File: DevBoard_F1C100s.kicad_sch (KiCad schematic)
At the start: 25 parts, among them J101 USB_C_Receptacle_USB2.0_16P, U101 F1C100s, U102 AMS1117, U103 AMS1117-3.3, U104 TPS562201DDCT

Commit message: Schematic: Finished
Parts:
- removed TP101: TestPoint_Small, TestPoint:TestPoint_Pad_D1.0mm, symbol Connector:TestPoint_Small
- added C108, C110, C113: 10uf, Capacitor_SMD:C_0603_1608Metric_Pad1.08x0.95mm_HandSolder, symbol Device:C_Small
- added C109, C112, C115, C116: 0.1uf, Capacitor_SMD:C_0603_1608Metric_Pad1.08x0.95mm_HandSolder, symbol Device:C_Small
- added C111, C114: 10pf, Capacitor_SMD:C_0603_1608Metric_Pad1.08x0.95mm_HandSolder, symbol Device:C_Small
- added J102: Conn_01x22, Connector_PinHeader_1.00mm:PinHeader_1x22_P1.00mm_Vertical_SMD_Pin1Left, symbol Connector_Generic:Conn_01x22
- added J103: Conn_01x11, Connector_PinHeader_1.00mm:PinHeader_1x11_P1.00mm_Vertical_SMD_Pin1Left, symbol Connector_Generic:Conn_01x11
- added J104: SD_Card, Connector_PinHeader_1.00mm:PinHeader_1x06_P1.00mm_Vertical_SMD_Pin1Left, symbol Connector_Generic:Conn_01x06
- added J105: UART0, Connector_PinHeader_1.00mm:PinHeader_1x04_P1.00mm_Vertical_SMD_Pin1Left, symbol Connector_Generic:Conn_01x04
- added J106: Conn_01x10, Connector_PinHeader_1.00mm:PinHeader_1x10_P1.00mm_Vertical_SMD_Pin1Left, symbol Connector_Generic:Conn_01x10
- added J107: Conn_01x04, Connector_PinHeader_1.00mm:PinHeader_1x04_P1.00mm_Vertical_SMD_Pin1Left, symbol Connector_Generic:Conn_01x04
- added J108: Conn_01x05, Connector_PinHeader_1.00mm:PinHeader_1x05_P1.00mm_Vertical_SMD_Pin1Left, symbol Connector_Generic:Conn_01x05
- added J109: Conn_01x02, Connector_PinHeader_1.00mm:PinHeader_1x02_P1.00mm_Vertical_SMD_Pin1Left, symbol Connector_Generic:Conn_01x02
- added R107: 10k, Resistor_SMD:R_0201_0603Metric_Pad0.64x0.40mm_HandSolder, symbol Device:R_Small
- added R108, R109, R110, R111, R112, R113: 5.1K, Resistor_SMD:R_0201_0603Metric_Pad0.64x0.40mm_HandSolder, symbol Device:R_Small
- added SW101, SW102: SW1, Button_Switch_SMD:SW_SPST_CK_RS282G05A3, symbol Switch:SW_Push
- added SW103: SW2, Button_Switch_SMD:SW_SPST_CK_RS282G05A3, symbol Switch:SW_Push
- added SW104: SW3, Button_Switch_SMD:SW_SPST_CK_RS282G05A3, symbol Switch:SW_Push
- added SW105: RESET, Button_Switch_SMD:SW_SPST_CK_RS282G05A3, symbol Switch:SW_Push
- added U104: W25Q16JVSS, Package_SO:SOIC-8_5.3x5.3mm_P1.27mm, symbol Memory_Flash:W25Q16JVSS
- added Y101: 24Mhz, Crystal:Crystal_SMD_3225-4Pin_3.2x2.5mm_HandSoldering, symbol Device:Crystal_GND24
- F101: footprint (none) -> Jumper:SolderJumper-2_P1.3mm_Open_TrianglePad1.0x1.5mm
- U103: renamed from U104; footprint DDC0006A_N -> TPS562201DDCT:DDC0006A_N
- U105: renamed from U101; footprint (none) -> F1C100s:QFN-88_EP_10x10_Pitch0.4mm
- renumbered C105 to C102, C107 to C103, C103 to C105, C102 to C106, C106 to C107, JP102 to JP101, R104 to R102, R102 to R103, R103 to R104, TP103 to TP101, TP104 to TP103, U102 to U101, U103 to U102
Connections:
- net 1V1: now also U105.22 (VCC_CORE), U105.35 (VCC_CORE), U105.71 (VCC_CORE), C113.1, C115.1
- net 2V6: now also U105.30 (VCC_DRAM), U105.31 (VCC_DRAM), U105.32 (VCC_DRAM), U105.34 (VCC_DRAM), U105.36 (VCC_DRAM), U105.80 (AVCC), C110.1, C112.1, R112.1
- net 3V3: now also U105.20 (VCC_IO), U105.4 (HPVCC), U105.5 (VCC_IO), U105.50 (VCC_IO), U105.73 (TV_VCC), C108.1, C109.1, J105.1 (Pin_1), R107.1, SW101.2, SW102.2, SW103.2, SW104.2, U104.3 (~{WP}/IO_{2}), U104.7 (~{HOLD}/~{RESET}/IO_{3}), U104.8 (VCC)
- net GND: now also U105.74 (TVGND), U105.82 (AGND), C108.2, C109.2, C110.2, C111.2, C112.2, C113.2, C114.1, C115.2, C116.2, J105.4 (Pin_4), R108.2, R109.2, R110.2, R111.2, R113.2, SW105.1, U104.4 (GND), Y101.2, Y101.4
- net PWR_F: now also U105.67 (USB_VCC)
- net USB_N: now also U105.68 (USB_DM)
- net USB_P: now also U105.69 (USB_DP)
- net HPL: now reaches U105.1 (HPL)
- net HPL: now also J106.8 (Pin_8)
- net PD4: now reaches U105.10 (PD4)
- net PD4: now also J102.5 (Pin_5)
- net PD5: now reaches U105.11 (PD5)
- net PD5: now also J102.6 (Pin_6)
- net PD6: now reaches U105.12 (PD6)
- net PD6: now also J102.7 (Pin_7)
- net PD7: now reaches U105.13 (PD7)
- net PD7: now also J102.8 (Pin_8)
- net PD8: now reaches U105.14 (PD8)
- net PD8: now also J102.9 (Pin_9)
- net PD9: now reaches U105.15 (PD9)
- net PD9: now also J102.10 (Pin_10)
- net PD10: now reaches U105.16 (PD10)
- net PD10: now also J102.11 (Pin_11)
- net PD11: now reaches U105.17 (PD11)
- net PD11: now also J102.12 (Pin_12)
- net PD12: now reaches U105.18 (PD12)
- net PD12: now also J102.13 (Pin_13)
- net PD13: now reaches U105.19 (PD13)
- net PD13: now also J102.14 (Pin_14)
- net HPCOMFB: now reaches U105.2 (HPCOMFB)
- net HPCOMFB: now also J106.10 (Pin_10)
- net PD14: now reaches U105.21 (PD14)
- net PD14: now also J102.15 (Pin_15)
- net PD15: now reaches U105.23 (PD15)
- net PD15: now also J102.16 (Pin_16)
- net PD16: now reaches U105.24 (PD16)
- net PD16: now also J102.17 (Pin_17)
- net PD17: now reaches U105.25 (PD17)
- net PD17: now also J102.18 (Pin_18)
- net PD18: now reaches U105.26 (PD18)
- net PD18: now also J102.19 (Pin_19)
- net PD19: now reaches U105.27 (PD19)
- net PD19: now also J102.20 (Pin_20)
- net PD20: now reaches U105.28 (PD20)
- net PD20: now also J102.21 (Pin_21)
- net PD21: now reaches U105.29 (PD21)
- net PD21: now also J102.22 (Pin_22)
- net HPCOM: now reaches U105.3 (HPCOM)
- net HPCOM: now also J106.9 (Pin_9)
- net SVREF: now reaches U105.33 (SVREF)
- net SVREF: now also J109.2 (Pin_2), R112.2, R113.1
- net SW3: now reaches U105.37 (PE12)
- net SW3: now also J103.11 (Pin_11), R111.1, SW104.1
- net SW2: now reaches U105.38 (PE11)
- net SW2: now also J103.10 (Pin_10), R110.1, SW103.1
- net SW1: now reaches U105.39 (PE10)
- net SW1: now also J103.9 (Pin_9), R109.1, SW102.1
- net SW0: now reaches U105.40 (PE9)
- net SW0: now also J103.8 (Pin_8), R108.1, SW101.1
- net PE8: now reaches U105.41 (PE8)
- net PE8: now also J103.7 (Pin_7)
- net PE7: now reaches U105.42 (PE7)
- net PE7: now also J103.6 (Pin_6)
- net PE6: now reaches U105.43 (PE6)
- net PE6: now also J103.5 (Pin_5)
- net PE5: now reaches U105.44 (PE5)
- net PE5: now also J103.4 (Pin_4)
- net PE4: now reaches U105.45 (PE4)
- net PE4: now also J103.3 (Pin_3)
- net PE3: now reaches U105.46 (PE3)
- net PE3: now also J103.2 (Pin_2)
- net PE2: now reaches U105.47 (PE2)
- net PE2: now also J103.1 (Pin_1)
- net UART0_TX: now reaches U105.48 (PE1)
- net UART0_TX: now also J105.3 (Pin_3)
- net UART0_RX: now reaches U105.49 (PE0)
- net UART0_RX: now also J105.2 (Pin_2)
- net HOSCI: now reaches U105.51 (HOSCI)
- net HOSCI: now also C111.1, Y101.1
- net HOSCO: now reaches U105.52 (HOSCO)
- net HOSCO: now also C114.2, Y101.3
- net SDC0_D2: now reaches U105.53 (PF5)
- net SDC0_D2: now also J104.6 (Pin_6)
- net SDC0_D3: now reaches U105.54 (PF4)
- net SDC0_D3: now also J104.5 (Pin_5)
- net SDC0_CMD: now reaches U105.55 (PF3)
- net SDC0_CMD: now also J104.4 (Pin_4)
- net SDC0_CLK: now reaches U105.56 (PF2)
- net SDC0_CLK: now also J104.3 (Pin_3)
- net SDC0_D0: now reaches U105.57 (PF1)
- net SDC0_D0: now also J104.2 (Pin_2)
- net SDC0_D1: now reaches U105.58 (PF0)
- net SDC0_D1: now also J104.1 (Pin_1)
- net SPI0_CLK: now reaches U105.59 (PC0)
- net SPI0_CLK: now also U104.6 (CLK)
- net PD0: now reaches U105.6 (PD0)
- net PD0: now also J102.1 (Pin_1)
- net SPI0_CS: now reaches U105.60 (PC1)
- net SPI0_CS: now also U104.1 (~{CS})
- net SPI0_MISO: now reaches U105.61 (PC2)
- net SPI0_MISO: now also U104.2 (DO/IO_{1})
- net SPI0_MOSI: now reaches U105.62 (PC3)
- net SPI0_MOSI: now also U104.5 (DI/IO_{0})
- net TPY2: now reaches U105.63 (TPY2)
- net TPY2: now also J107.1 (Pin_1)
- net TPY1: now reaches U105.64 (TPY1)
- net TPY1: now also J107.2 (Pin_2)
- net TPX2: now reaches U105.65 (TPX2)
- net TPX2: now also J107.3 (Pin_3)
- net TPX1: now reaches U105.66 (TPX1)
- net TPX1: now also J107.4 (Pin_4)
- net PD1: now reaches U105.7 (PD1)
- net PD1: now also J102.2 (Pin_2)
- net RESET: now reaches U105.70 (RESET)
- net RESET: now also C116.1, R107.2, SW105.2
- net TVOUT: now reaches U105.72 (TVOUT)
- net TVOUT: now also J108.1 (Pin_1)
- net TV_VRN: now reaches U105.75 (TV_VRN)
- net TV_VRN: now also J108.2 (Pin_2)
- net TV_VRP: now reaches U105.76 (TV_VRP)
- net TV_VRP: now also J108.3 (Pin_3)
- net TVIN1: now reaches U105.77 (TVIN1)
- net TVIN1: now also J108.4 (Pin_4)
- net TVIN0: now reaches U105.78 (TVIN0)
- net TVIN0: now also J108.5 (Pin_5)
- net LRADC0: now reaches U105.79 (LRADC0)
- net LRADC0: now also J109.1 (Pin_1)
- net PD2: now reaches U105.8 (PD2)
- net PD2: now also J102.3 (Pin_3)
- net VRA1: now reaches U105.81 (VRA1)
- net VRA1: now also J106.1 (Pin_1)
- net VRA2: now reaches U105.83 (VRA2)
- net VRA2: now also J106.2 (Pin_2)
- net FMINL: now reaches U105.84 (FMINL)
- net FMINL: now also J106.3 (Pin_3)
- net FMINR: now reaches U105.85 (FMINR)
- net FMINR: now also J106.4 (Pin_4)
- net LINL: now reaches U105.86 (LINL)
- net LINL: now also J106.5 (Pin_5)
- net MICIN: now reaches U105.87 (MICIN)
- net MICIN: now also J106.6 (Pin_6)
- net HPR: now reaches U105.88 (HPR)
- net HPR: now also J106.7 (Pin_7)
- net PD3: now reaches U105.9 (PD3)
- net PD3: now also J102.4 (Pin_4)
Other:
- note added: "Power VCORE: 1.1V 2A VIO: 3.3V 1A VDRAM: 2.6V 1A"
- moved on the sheet: U105

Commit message: Routing: WIP
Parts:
- removed J107: Conn_01x04, Connector_PinHeader_1.00mm:PinHeader_1x04_P1.00mm_Vertical_SMD_Pin1Left, symbol Connector_Generic:Conn_01x04
- removed TP101, TP102, TP103: TestPoint_Small, TestPoint:TestPoint_Pad_D1.0mm, symbol Connector:TestPoint_Small
- R101, R102, R103, R104, R105, R106, R107, R108, R109, R110, R111, R112, R113: footprint Resistor_SMD:R_0201_0603Metric_Pad0.64x0.40mm_HandSolder -> Resistor_SMD:R_0603_1608Metric_Pad0.98x0.95mm_HandSolder
- SW101: value SW1 -> SW0
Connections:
- net TPX1: no longer names the net of U105.66 (TPX1)
- net TPX2: no longer names the net of U105.65 (TPX2)
- net TPY1: no longer names the net of U105.64 (TPY1)
- net TPY2: no longer names the net of U105.63 (TPY2)
- no-connect marks 2 -> 6

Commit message: Layout: Almost complete
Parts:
- removed F101: 5V 2A, Jumper:SolderJumper-2_P1.3mm_Open_TrianglePad1.0x1.5mm, symbol Device:Polyfuse_Small
- removed J109: Conn_01x02, Connector_PinHeader_1.00mm:PinHeader_1x02_P1.00mm_Vertical_SMD_Pin1Left, symbol Connector_Generic:Conn_01x02
- added TP1, TP2: TestPoint, TestPoint:TestPoint_Pad_D1.0mm, symbol Connector:TestPoint
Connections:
- net VBUS is gone; now on net VUSB: J101.A4 (VBUS), J101.A9 (VBUS), J101.B4 (VBUS), J101.B9 (VBUS)
- net LRADC0: now also TP1.1
- net SVREF: now also TP2.1
- net PWR_F renamed VUSB

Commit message: Finish design
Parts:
- removed J104: SD_Card, Connector_PinHeader_1.00mm:PinHeader_1x06_P1.00mm_Vertical_SMD_Pin1Left, symbol Connector_Generic:Conn_01x06
- added J104: Micro_SD_Card_Det1, sd_card:sd_card_10p, symbol sd_card:Micro_SD_Card_Det1
- added R114, R115, R116, R117, R118, R119: 10k, Resistor_SMD:R_0603_1608Metric_Pad0.98x0.95mm_HandSolder, symbol Device:R_Small
- added TP3: TestPoint, TestPoint:TestPoint_Pad_D1.0mm, symbol Connector:TestPoint
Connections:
- net 3V3: now also J104.4 (VDD), R114.1, R115.1, R116.1, R117.1, R118.1, R119.1
- net GND: now also J104.10 (SHIELD), J104.6 (VSS)
- net SDC0_CLK: now also J104.5 (CLK), R117.2
- net SDC0_CMD: now also J104.3 (CMD), R116.2
- net SDC0_D0: now also J104.7 (DAT0), R118.2
- net SDC0_D1: now also J104.8 (DAT1), R119.2
- net SDC0_D2: now also J104.1 (DAT2), R114.2
- net SDC0_D3: now also J104.2 (DAT3/CD), R115.2
- new net: J104.9 (DET), TP3.1
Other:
- moved on the sheet: C111, C114, J105, R112, R113, TP1, TP2, Y101

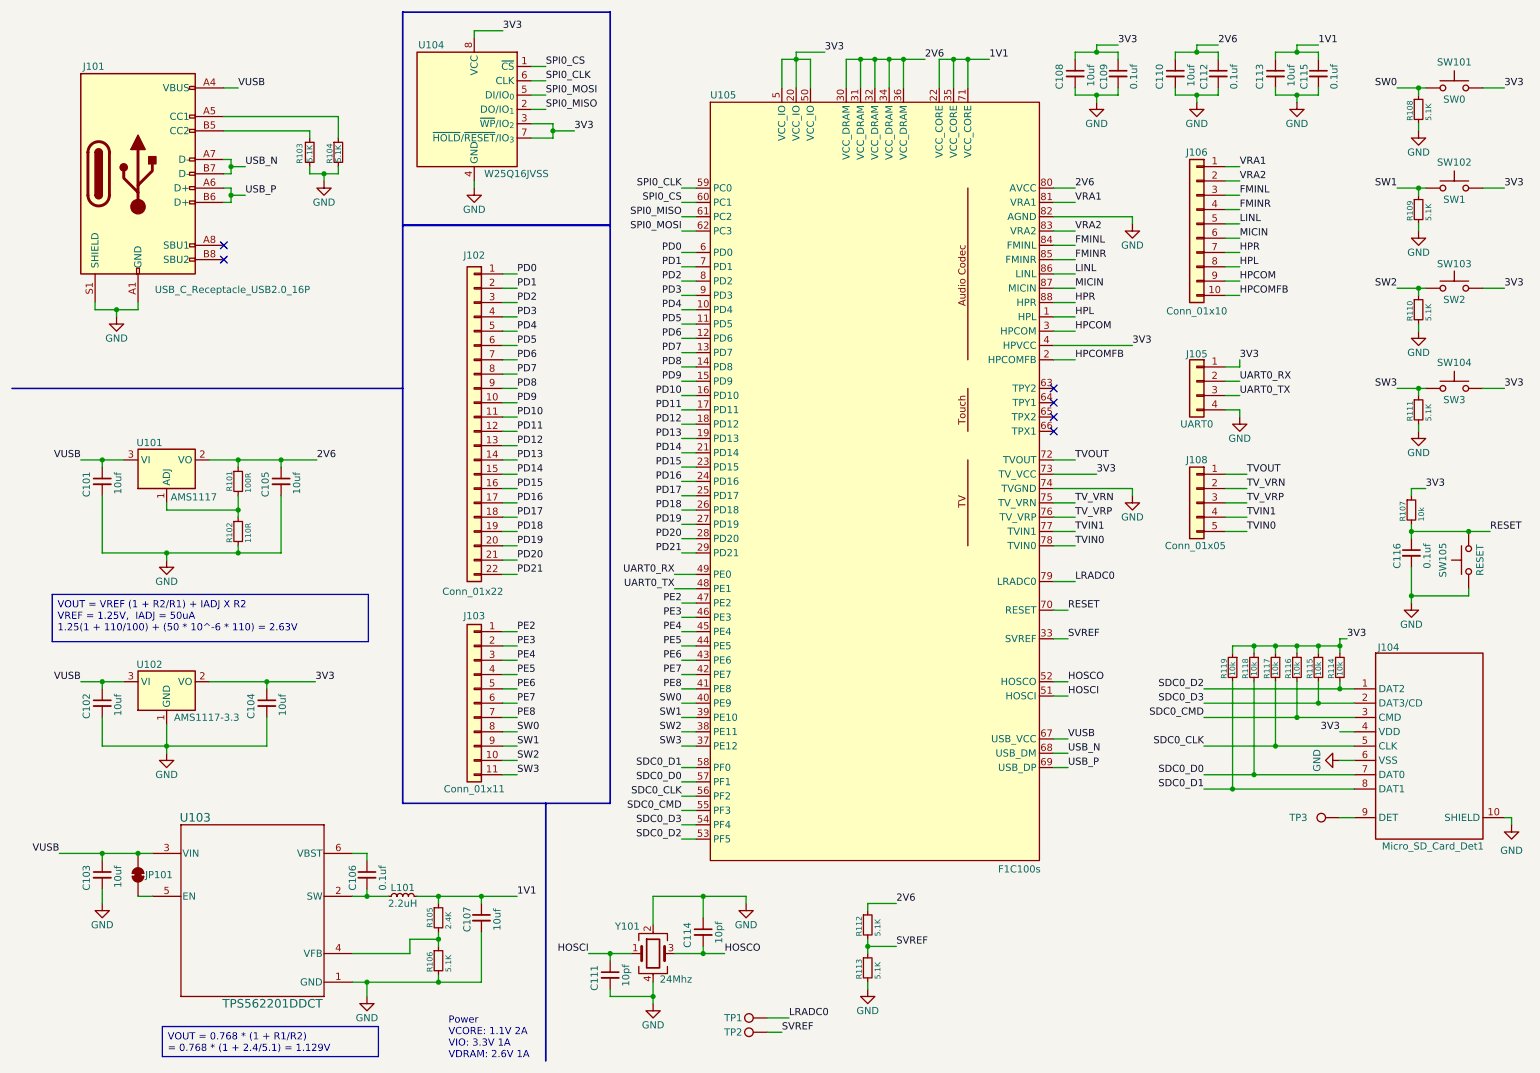
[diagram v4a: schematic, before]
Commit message: Fix ground pour clearance
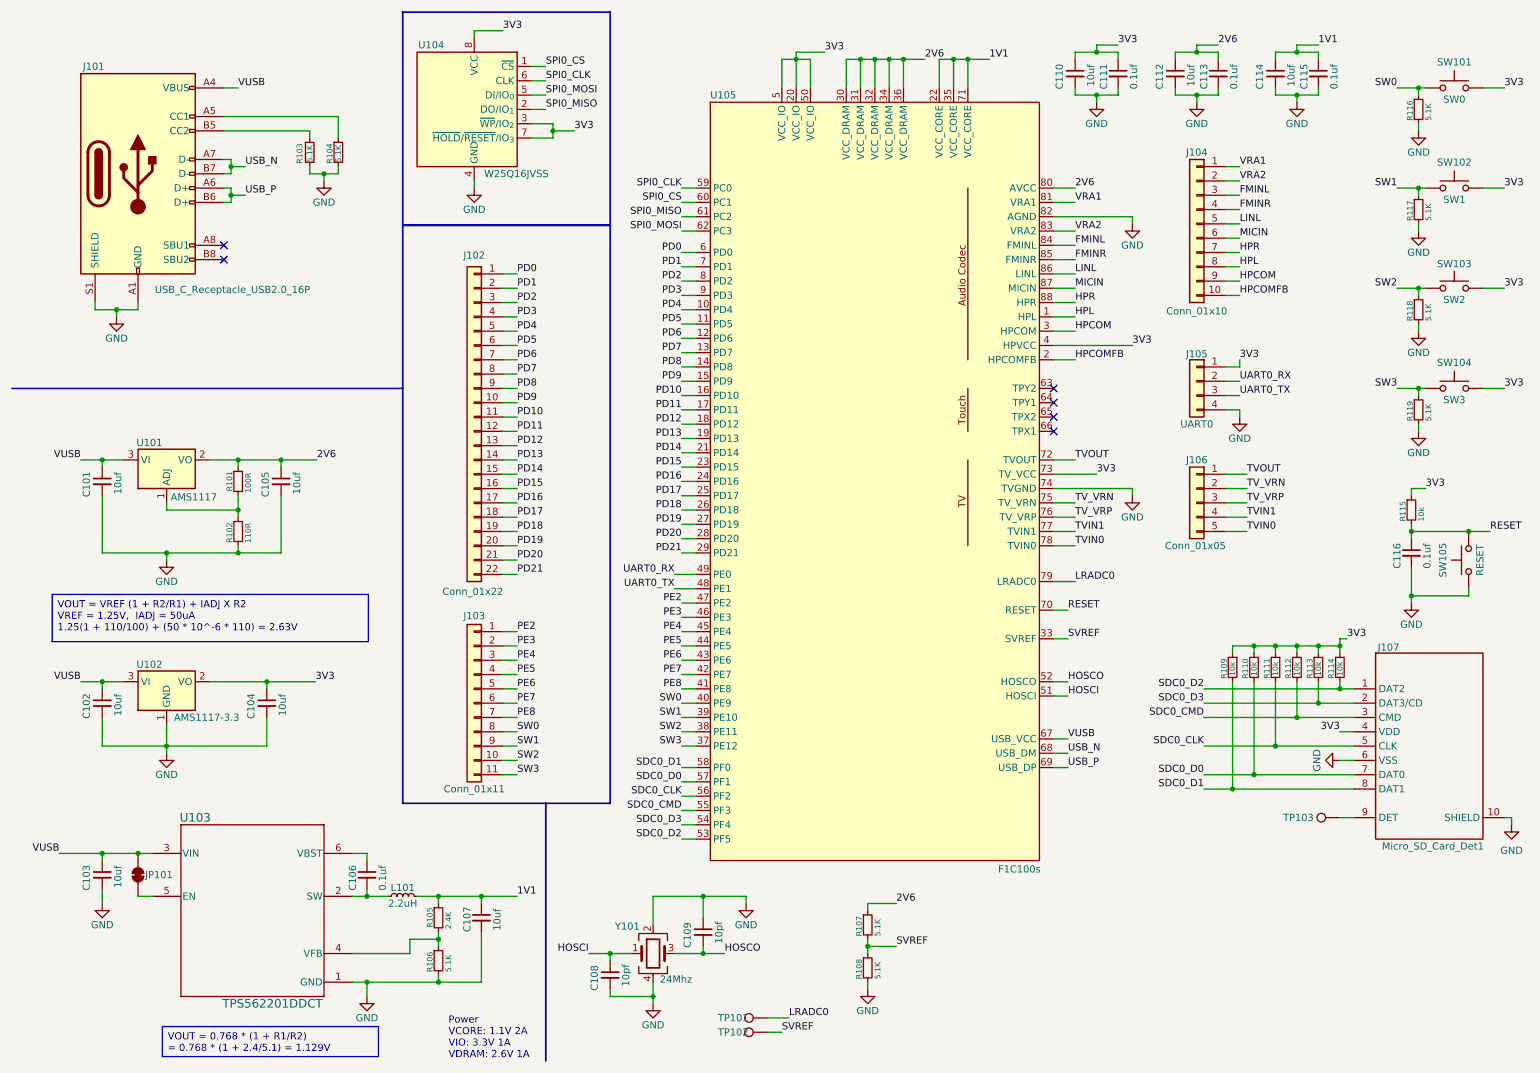
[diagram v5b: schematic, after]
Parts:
- renumbered C111 to C108, C114 to C109, C108 to C110, C109 to C111, C110 to C112, C112 to C113, C113 to C114, J106 to J104, J108 to J106, J104 to J107, R112 to R107, R113 to R108, R119 to R109, R118 to R110, R117 to R111, R116 to R112, R115 to R113, R107 to R115, R108 to R116, R109 to R117, R110 to R118, R111 to R119, TP1 to TP101, TP2 to TP102, TP3 to TP103
